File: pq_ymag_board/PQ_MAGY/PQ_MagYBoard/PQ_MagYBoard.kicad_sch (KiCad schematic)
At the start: 14 parts, among them J1 M20-7810245

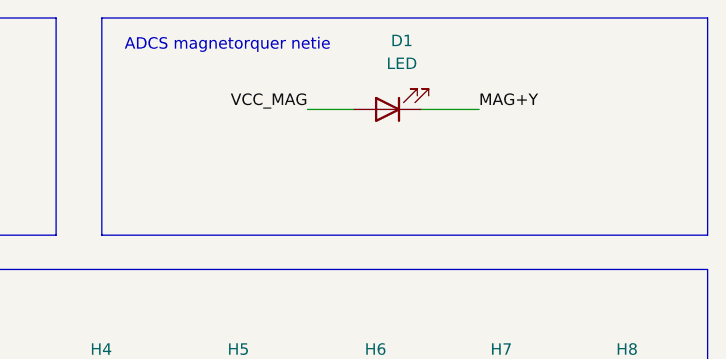
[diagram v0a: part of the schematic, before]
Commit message: Removed photodiode +Y magnetorquer PCB
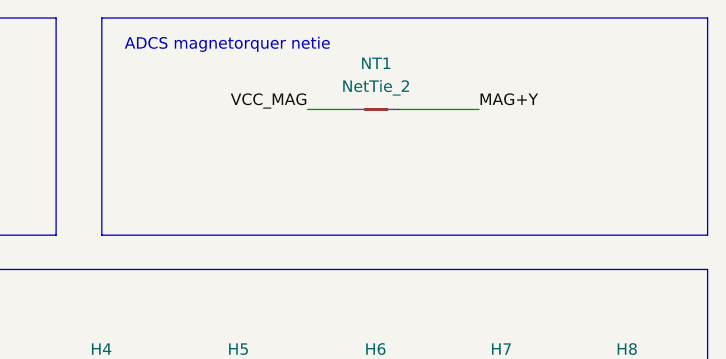
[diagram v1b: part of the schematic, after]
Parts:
- removed D1: LED, LED_SMD:LED_0402_1005Metric, symbol Device:LED
- added NT1: NetTie_2, NetTie:NetTie-2_SMD_Pad0.5mm, symbol Device:NetTie_2
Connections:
- net MAG+Y: now also NT1.2
- net VCC_MAG: now also NT1.1

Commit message: ADCS_HBRIDGE backup restore
Restored version with H bridge and no connectors modification
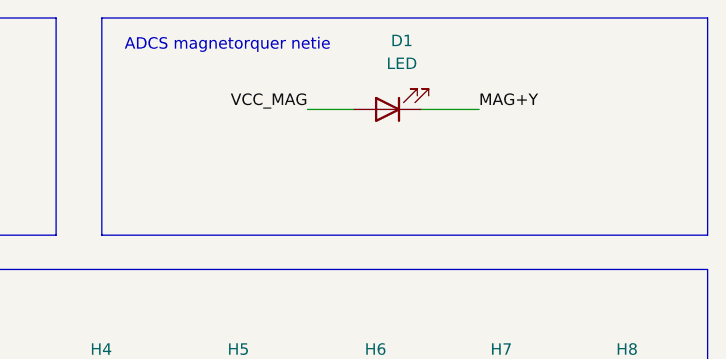
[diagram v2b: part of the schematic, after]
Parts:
- removed NT1: NetTie_2, NetTie:NetTie-2_SMD_Pad0.5mm, symbol Device:NetTie_2
- added D1: LED, LED_SMD:LED_0402_1005Metric, symbol Device:LED
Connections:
- net MAG+Y: now also D1.1 (K)
- net VCC_MAG: now also D1.2 (A)
